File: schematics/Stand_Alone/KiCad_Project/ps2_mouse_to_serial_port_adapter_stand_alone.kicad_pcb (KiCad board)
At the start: 2 copper layers, 90 x 70 mm, 28 parts, among them J1 2.1 Barrel Jack, J2 DB9 Female, J3 Mini-DIN-6, Q1 BC547, SW1 1C2P, U1 74LS00, U2 L78L05, U3 L7805

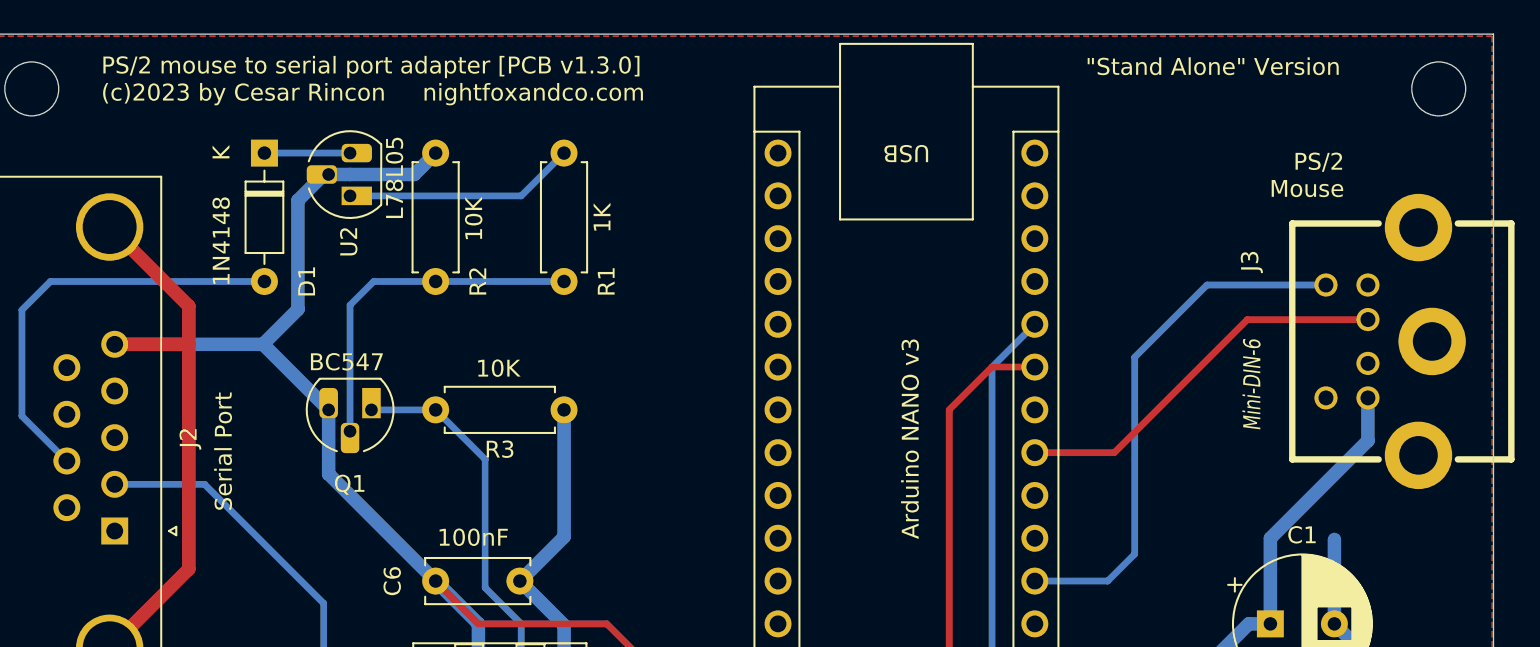
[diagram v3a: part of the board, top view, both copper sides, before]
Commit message: v1.7.1
- Wrong files upload fix.
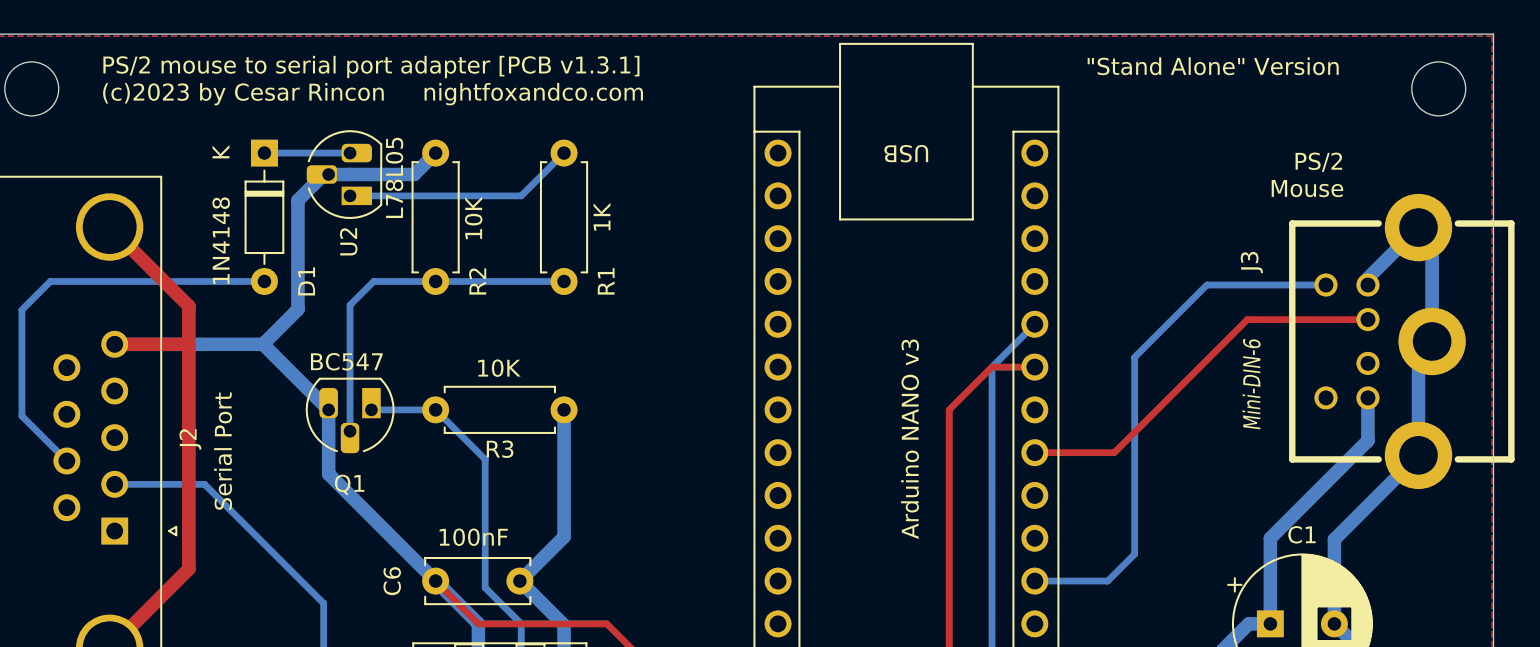
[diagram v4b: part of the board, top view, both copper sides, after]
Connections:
- J3 pad GND: (no net) -> /GND
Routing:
- net /GND: track 269.9 -> 293.1 mm
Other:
- board text added: "PS/2 mouse to serial port adapter [PCB v1.3.1] (c)2023 by Cesar Rincon nightfoxandco.com"
- board text removed: "PS/2 mouse to serial port adapter [PCB v1.3.0] (c)2023 by Cesar Rincon nightfoxandco.com"
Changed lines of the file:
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@@
     (pad "6" thru_hole circle (at 3.35026 11.00074 90) (size 1.3716 1.3716) (drill 0.889) (layers "*.Cu" "*.Mask")
       (net 43 "unconnected-(J3-Pad6)") (pintype "passive+no_connect"))
-    (pad "GND" thru_hole circle (at -6.75894 5.50926 90) (size 4.0005 4.0005) (drill 2.29108) (layers "*.Cu" "*.Mask"))
-    (pad "GND" thru_hole circle (at 0 4.699 90) (size 4.0005 4.0005) (drill 2.29108) (layers "*.Cu" "*.Mask"))
-    (pad "GND" thru_hole circle (at 6.75894 5.50926 90) (size 4.0005 4.0005) (drill 2.29108) (layers "*.Cu" "*.Mask"))
+    (pad "GND" thru_hole circle (at -6.75894 5.50926 90) (size 4.0005 4.0005) (drill 2.29108) (layers "*.Cu" "*.Mask")
+      (net 3 "/GND"))
+    (pad "GND" thru_hole circle (at 0 4.699 90) (size 4.0005 4.0005) (drill 2.29108) (layers "*.Cu" "*.Mask")
+      (net 3 "/GND"))
+    (pad "GND" thru_hole circle (at 6.75894 5.50926 90) (size 4.0005 4.0005) (drill 2.29108) (layers "*.Cu" "*.Mask")
+      (net 3 "/GND"))
     (model "r_mini_dins/minidin_6.wrl"
       (offset (xyz 0 0 0))
@@
     (effects (font (size 1 1) (thickness 0.1)) (justify left bottom))
   )
-  (gr_text "PS/2 mouse to serial port adapter [PCB v1.3.0]\n(c)2023 by Cesar Rincon     nightfoxandco.com" (at 30.226 18.034) (layer "F.SilkS")
+  (gr_text "PS/2 mouse to serial port adapter [PCB v1.3.1]\n(c)2023 by Cesar Rincon     nightfoxandco.com" (at 30.226 18.034) (layer "F.SilkS")
     (effects (font (size 1 1) (thickness 0.1)) (justify left bottom))
   )
@@
   (segment (start 85.64 79.45) (end 105.96 79.45) (width 0.8) (layer "B.Cu") (net 3))
   (segment (start 107.2465 78.1635) (end 108.5 76.91) (width 0.8) (layer "B.Cu") (net 3))
-  (segment (start 103.42 48.97) (end 103.42 43.95842) (width 0.8) (layer "B.Cu") (net 3))
   (segment (start 55.08 79.37) (end 57.7 81.99) (width 0.8) (layer "B.Cu") (net 3))
   (segment (start 108.5 64.21) (end 108.5 71.83) (width 0.8) (layer "B.Cu") (net 3))
@@
   (segment (start 52.62 64.21) (end 50.08 66.75) (width 0.8) (layer "B.Cu") (net 3))
   (segment (start 50.08 21.03) (end 48.81 22.3) (width 0.8) (layer "B.Cu") (net 3))
+  (segment (start 108.40974 38.96868) (end 108.40974 33.02) (width 0.8) (layer "B.Cu") (net 3))
   (segment (start 39.92 79.45) (end 50 79.45) (width 0.8) (layer "B.Cu") (net 3))
   (segment (start 52.62 48.97) (end 52.62 64.21) (width 0.8) (layer "B.Cu") (net 3))
+  (segment (start 108.40974 25.4508) (end 105.41 28.45054) (width 0.8) (layer "B.Cu") (net 3))
   (segment (start 27.48 75.39) (end 27.48 68.96) (width 0.8) (layer "B.Cu") (net 3))
   (segment (start 108.5 64.21) (end 108.5 54.05) (width 0.8) (layer "B.Cu") (net 3))
+  (segment (start 109.22 32.20974) (end 109.22 26.26106) (width 0.8) (layer "B.Cu") (net 3))
+  (segment (start 103.42 43.95842) (end 108.40974 38.96868) (width 0.8) (layer "B.Cu") (net 3))
   (segment (start 43.45 22.3) (end 45 22.3) (width 0.8) (layer "B.Cu") (net 3))
   (segment (start 31.444 79.45) (end 27.432 75.438) (width 0.8) (layer "B.Cu") (net 3))
@@
   (segment (start 62.78 81.99) (end 67.86 81.99) (width 0.8) (layer "B.Cu") (net 3))
   (segment (start 108.5 76.91) (end 108.5 71.83) (width 0.8) (layer "B.Cu") (net 3))
+  (segment (start 103.42 48.97) (end 103.42 43.95842) (width 0.8) (layer "B.Cu") (net 3))
   (segment (start 43.73 40.08) (end 50.08 46.43) (width 0.8) (layer "B.Cu") (net 3))
   (segment (start 39.92 56.59) (end 28.627 56.59) (width 0.8) (layer "B.Cu") (net 4))
